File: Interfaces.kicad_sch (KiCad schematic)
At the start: 2 parts, among them J5 Conn_01x05_Pin, J6 Conn_01x05_Pin

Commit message: LCD connector, backlight, other work
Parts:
- removed J5: Conn_01x05_Pin, Connector_Molex:Molex_Micro-Fit_3.0_43650-0515_1x05_P3.00mm_Vertical, symbol Connector:Conn_01x05_Pin
- added J3: Conn_02x02_Counter_Clockwise, Connector_Molex:Molex_Micro-Fit_3.0_43045-0412_2x02_P3.00mm_Vertical, symbol Connector_Generic:Conn_02x02_Counter_Clockwise
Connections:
- net GND: now also J3.1 (Pin_1)
- new net +5V: J3.2 (Pin_2)
- new net IO_D0: J3.3 (Pin_3)
- new net IO_D1: J3.4 (Pin_4)
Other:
- moved on the sheet: J6

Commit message: preliminary complete schematic
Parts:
- removed J3: Conn_02x02_Counter_Clockwise, Connector_Molex:Molex_Micro-Fit_3.0_43045-0412_2x02_P3.00mm_Vertical, symbol Connector_Generic:Conn_02x02_Counter_Clockwise
- removed J6: Conn_01x05_Pin, Connector_Molex:Molex_Micro-Fit_3.0_43650-0515_1x05_P3.00mm_Vertical, symbol Connector:Conn_01x05_Pin
- added C12: 100n, Capacitor_SMD:C_0603_1608Metric_Pad1.08x0.95mm_HandSolder, symbol Device:C
- added C31, C32: 1u, Capacitor_SMD:C_0603_1608Metric_Pad1.08x0.95mm_HandSolder, symbol Device:C
- added J1: Conn_01x05_MountingPin, Connector_Molex:Molex_Micro-Fit_3.0_43650-0510_1x05-1MP_P3.00mm_Horizontal, symbol Connector_Generic_MountingPin:Conn_01x05_MountingPin
- added J3: Conn_01x04_MountingPin, Connector_Molex:Molex_Micro-Fit_3.0_43650-0410_1x04-1MP_P3.00mm_Horizontal, symbol Connector_Generic_MountingPin:Conn_01x04_MountingPin
- added J4: MSD-11-A, SamacSys_Parts:MSD11A, symbol SamacSys_Parts:MSD-11-A
- added J5: Conn_01x05_Pin, Connector_PinHeader_2.54mm:PinHeader_1x05_P2.54mm_Vertical, symbol Connector:Conn_01x05_Pin
- added R16, R17, R18, R19, R20, R22, R24, R27: 5.1k, Resistor_SMD:R_0603_1608Metric_Pad0.98x0.95mm_HandSolder, symbol Device:R
- added U6: TLV74033PDBVR, SamacSys_Parts:SOT95P280X145-5N, symbol SamacSys_Parts:TLV74033PDBVR
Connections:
- net +12V_IN: now also J1.2 (Pin_2)
- net +5V: now also C31.1, U6.1 (IN), U6.3 (EN)
- net +5V_BUS: now also J1.3 (Pin_3)
- net GND: now also C12.2, C31.2, C32.2, J1.1 (Pin_1), J1.MP (MountPin), J3.1 (Pin_1), J3.MP (MountPin), J4.G1 (GND_1), J4.G2 (GND_2), J4.P6 (VSS), J5.1 (Pin_1), U6.2 (GND)
- net PRIMARY_CAN+: now also J1.4 (Pin_4)
- net PRIMARY_CAN-: now also J1.5 (Pin_5)
- new net +3.3V: C12.1, J4.P4 (VDD), R16.2, R17.2, R18.2, R19.2, R20.2, R22.2, R24.2, R27.2
- new net +3.3V_AUX: C32.1, J3.2 (Pin_2), J5.2 (Pin_2), U6.5 (OUT)
- new net DPAD_A0: J3.3 (Pin_3)
- new net DPAD_A1: J3.4 (Pin_4)
- new net I2S_BCLK: J5.5 (Pin_5)
- new net I2S_SD: J5.4 (Pin_4)
- new net I2S_WS: J5.3 (Pin_3)
- new net SD_CD: J4.P9 (CD), R27.1
- new net SD_CLK: J4.P5 (CLK), R18.1
- new net SD_CMD: J4.P3 (CMD), R19.1
- new net SD_CS: J4.P2 (CD/DAT3), R20.1
- new net SD_D0: J4.P7 (DAT0), R17.1
- new net SD_D1: J4.P8 (DAT1), R16.1
- new net SD_D2: J4.P1 (DAT2), R22.1
- new net SD_WP: J4.P10 (WP), R24.1

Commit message: basic layout organization, fix +VDDA typo
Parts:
- renumbered C31 to C18, C32 to C19, C12 to C20, J5 to J4, J1 to J5, J4 to J6, R19 to R10, R20 to R11, R22 to R12, R24 to R13, R27 to R14, R16 to R7, R17 to R8, R18 to R9, U6 to U3
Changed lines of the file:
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@@
 		(on_board yes)
 		(dnp no)
-		(property "Reference" "J1"
+		(property "Reference" "J5"
 			(at 186.69 40.9955 0)
 			(effects
@@
 			(project ""
 				(path "/f2bb7816-6b2a-47fd-8906-eb4aedd6f9e6/61479cd4-0d84-48d3-a2a5-35c815fbc6c8"
-					(reference "J1")
+					(reference "J5")
 					(unit 1)
 				)
@@
 		(dnp no)
 		(fields_autoplaced yes)
-		(property "Reference" "#PWR026"
+		(property "Reference" "#PWR027"
 			(at 222.25 48.26 0)
 			(effects
@@
 			(project "LV3-Core"
 				(path "/f2bb7816-6b2a-47fd-8906-eb4aedd6f9e6/61479cd4-0d84-48d3-a2a5-35c815fbc6c8"
-					(reference "#PWR026")
+					(reference "#PWR027")
 					(unit 1)
 				)
@@
 		(dnp no)
 		(fields_autoplaced yes)
-		(property "Reference" "#PWR055"
+		(property "Reference" "#PWR032"
 			(at 222.25 78.74 0)
 			(effects
@@
 			(project "LV3-Dash"
 				(path "/f2bb7816-6b2a-47fd-8906-eb4aedd6f9e6/61479cd4-0d84-48d3-a2a5-35c815fbc6c8"
-					(reference "#PWR055")
+					(reference "#PWR032")
 					(unit 1)
 				)
@@
 		(dnp no)
 		(fields_autoplaced yes)
-		(property "Reference" "R18"
+		(property "Reference" "R9"
 			(at 118.11 104.1399 0)
 			(effects
@@
 			(project "LV3-Dash"
 				(path "/f2bb7816-6b2a-47fd-8906-eb4aedd6f9e6/61479cd4-0d84-48d3-a2a5-35c815fbc6c8"
-					(reference "R18")
+					(reference "R9")
 					(unit 1)
 				)
@@
 		(dnp no)
 		(fields_autoplaced yes)
-		(property "Reference" "#PWR060"
+		(property "Reference" "#PWR028"
 			(at 120.65 54.61 0)
 			(effects
@@
 			(project "LV3-Dash"
 				(path "/f2bb7816-6b2a-47fd-8906-eb4aedd6f9e6/61479cd4-0d84-48d3-a2a5-35c815fbc6c8"
-					(reference "#PWR060")
+					(reference "#PWR028")
 					(unit 1)
 				)
@@
 		(dnp no)
 		(fields_autoplaced yes)
-		(property "Reference" "R27"
+		(property "Reference" "R14"
 			(at 165.1 104.1399 0)
 			(effects
@@
 			(project "LV3-Dash"
 				(path "/f2bb7816-6b2a-47fd-8906-eb4aedd6f9e6/61479cd4-0d84-48d3-a2a5-35c815fbc6c8"
-					(reference "R27")
+					(reference "R14")
 					(unit 1)
 				)
@@
 		(dnp no)
 		(fields_autoplaced yes)
-		(property "Reference" "R19"
+		(property "Reference" "R10"
 			(at 128.27 104.1399 0)
 			(effects
@@
 			(project "LV3-Dash"
 				(path "/f2bb7816-6b2a-47fd-8906-eb4aedd6f9e6/61479cd4-0d84-48d3-a2a5-35c815fbc6c8"
-					(reference "R19")
+					(reference "R10")
 					(unit 1)
 				)
@@
 		(dnp no)
 		(fields_autoplaced yes)
-		(property "Reference" "J5"
+		(property "Reference" "J4"
 			(at 239.395 30.48 0)
 			(effects
@@
 			(project ""
 				(path "/f2bb7816-6b2a-47fd-8906-eb4aedd6f9e6/61479cd4-0d84-48d3-a2a5-35c815fbc6c8"
-					(reference "J5")
+					(reference "J4")
 					(unit 1)
 				)
@@
 		(dnp no)
 		(fields_autoplaced yes)
-		(property "Reference" "U6"
+		(property "Reference" "U3"
 			(at 203.2 64.77 0)
 			(effects
@@
 			(project "LV3-Dash"
 				(path "/f2bb7816-6b2a-47fd-8906-eb4aedd6f9e6/61479cd4-0d84-48d3-a2a5-35c815fbc6c8"
-					(reference "U6")
+					(reference "U3")
 					(unit 1)
 				)
@@
 		(dnp no)
 		(fields_autoplaced yes)
-		(property "Reference" "#PWR050"
+		(property "Reference" "#PWR029"
 			(at 259.08 54.61 0)
 			(effects
@@
 			(project "LV3-Dash"
 				(path "/f2bb7816-6b2a-47fd-8906-eb4aedd6f9e6/61479cd4-0d84-48d3-a2a5-35c815fbc6c8"
-					(reference "#PWR050")
+					(reference "#PWR029")
 					(unit 1)
 				)
@@
 		(dnp no)
 		(fields_autoplaced yes)
-		(property "Reference" "J4"
+		(property "Reference" "J6"
 			(at 57.15 104.14 0)
 			(effects
@@
 			(project "LV3-Dash"
 				(path "/f2bb7816-6b2a-47fd-8906-eb4aedd6f9e6/61479cd4-0d84-48d3-a2a5-35c815fbc6c8"
-					(reference "J4")
+					(reference "J6")
 					(unit 1)
 				)
@@
 		(dnp no)
 		(fields_autoplaced yes)
-		(property "Reference" "#PWR015"
+		(property "Reference" "#PWR023"
 			(at 135.89 35.56 0)
 			(effects
@@
 			(project "LV3-Dash"
 				(path "/f2bb7816-6b2a-47fd-8906-eb4aedd6f9e6/61479cd4-0d84-48d3-a2a5-35c815fbc6c8"
-					(reference "#PWR015")
+					(reference "#PWR023")
 					(unit 1)
 				)
@@
 		(dnp no)
 		(fields_autoplaced yes)
-		(property "Reference" "#PWR054"
+		(property "Reference" "#PWR033"
 			(at 187.96 88.9 0)
 			(effects
@@
 			(project "LV3-Dash"
 				(path "/f2bb7816-6b2a-47fd-8906-eb4aedd6f9e6/61479cd4-0d84-48d3-a2a5-35c815fbc6c8"
-					(reference "#PWR054")
+					(reference "#PWR033")
 					(unit 1)
 				)
@@
 		(dnp no)
 		(fields_autoplaced yes)
-		(property "Reference" "R24"
+		(property "Reference" "R13"
 			(at 156.21 104.1399 0)
 			(effects
@@
 			(project "LV3-Dash"
 				(path "/f2bb7816-6b2a-47fd-8906-eb4aedd6f9e6/61479cd4-0d84-48d3-a2a5-35c815fbc6c8"
-					(reference "R24")
+					(reference "R13")
 					(unit 1)
 				)
@@
 		(dnp no)
 		(fields_autoplaced yes)
-		(property "Reference" "C32"
+		(property "Reference" "C19"
 			(at 226.06 77.4699 0)
 			(effects
@@
 			(project "LV3-Dash"
 				(path "/f2bb7816-6b2a-47fd-8906-eb4aedd6f9e6/61479cd4-0d84-48d3-a2a5-35c815fbc6c8"
-					(reference "C32")
+					(reference "C19")
 					(unit 1)
 				)
@@
 		(dnp no)
 		(fields_autoplaced yes)
-		(property "Reference" "R17"
+		(property "Reference" "R8"
 			(at 109.22 104.1399 0)
 			(effects
@@
 			(project "LV3-Dash"
 				(path "/f2bb7816-6b2a-47fd-8906-eb4aedd6f9e6/61479cd4-0d84-48d3-a2a5-35c815fbc6c8"
-					(reference "R17")
+					(reference "R8")
 					(unit 1)
 				)
@@
 		(dnp no)
 		(fields_autoplaced yes)
-		(property "Reference" "R20"
+		(property "Reference" "R11"
 			(at 138.43 104.1399 0)
 			(effects
@@
 			(project "LV3-Dash"
 				(path "/f2bb7816-6b2a-47fd-8906-eb4aedd6f9e6/61479cd4-0d84-48d3-a2a5-35c815fbc6c8"
-					(reference "R20")
+					(reference "R11")
 					(unit 1)
 				)
@@
 		(dnp no)
 		(fields_autoplaced yes)
-		(property "Reference" "#PWR051"
+		(property "Reference" "#PWR031"
 			(at 170.18 76.2 0)
 			(effects
@@
 			(project "LV3-Dash"
 				(path "/f2bb7816-6b2a-47fd-8906-eb4aedd6f9e6/61479cd4-0d84-48d3-a2a5-35c815fbc6c8"
-					(reference "#PWR051")
+					(reference "#PWR031")
 					(unit 1)
 				)
@@
 		(dnp no)
 		(fields_autoplaced yes)
-		(property "Reference" "#PWR061"
+		(property "Reference" "#PWR030"
 			(at 189.23 58.42 0)
 			(effects
@@
 			(project "LV3-Dash"
 				(path "/f2bb7816-6b2a-47fd-8906-eb4aedd6f9e6/61479cd4-0d84-48d3-a2a5-35c815fbc6c8"
-					(reference "#PWR061")
+					(reference "#PWR030")
 					(unit 1)
 				)
@@
 		(dnp no)
 		(fields_autoplaced yes)
-		(property "Reference" "#PWR027"
+		(property "Reference" "#PWR036"
 			(at 34.29 124.46 0)
 			(effects
@@
 			(project "LV3-Dash"
 				(path "/f2bb7816-6b2a-47fd-8906-eb4aedd6f9e6/61479cd4-0d84-48d3-a2a5-35c815fbc6c8"
-					(reference "#PWR027")
+					(reference "#PWR036")
 					(unit 1)
 				)
@@
 		(dnp no)
 		(fields_autoplaced yes)
-		(property "Reference" "#PWR046"
+		(property "Reference" "#PWR022"
 			(at 261.62 34.29 0)
 			(effects
@@
 			(project "LV3-Dash"
 				(path "/f2bb7816-6b2a-47fd-8906-eb4aedd6f9e6/61479cd4-0d84-48d3-a2a5-35c815fbc6c8"
-					(reference "#PWR046")
+					(reference "#PWR022")
 					(unit 1)
 				)
@@
 		(dnp no)
 		(fields_autoplaced yes)
-		(property "Reference" "C12"
+		(property "Reference" "C20"
 			(at 77.47 96.5199 0)
 			(effects
@@
 			(project "LV3-Dash"
 				(path "/f2bb7816-6b2a-47fd-8906-eb4aedd6f9e6/61479cd4-0d84-48d3-a2a5-35c815fbc6c8"
-					(reference "C12")
+					(reference "C20")
 					(unit 1)
 				)
@@
 		(dnp no)
 		(fields_autoplaced yes)
-		(property "Reference" "#PWR029"
+		(property "Reference" "#PWR035"
 			(at 81.28 107.95 0)
 			(effects
@@
 			(project "LV3-Dash"
 				(path "/f2bb7816-6b2a-47fd-8906-eb4aedd6f9e6/61479cd4-0d84-48d3-a2a5-35c815fbc6c8"
-					(reference "#PWR029")
+					(reference "#PWR035")
 					(unit 1)
 				)
@@
 		(dnp no)
 		(fields_autoplaced yes)
-		(property "Reference" "#PWR028"
+		(property "Reference" "#PWR034"
 			(at 87.63 97.79 0)
 			(effects
@@
 			(project "LV3-Dash"
 				(path "/f2bb7816-6b2a-47fd-8906-eb4aedd6f9e6/61479cd4-0d84-48d3-a2a5-35c815fbc6c8"
-					(reference "#PWR028")
+					(reference "#PWR034")
 					(unit 1)
 				)
@@
 		(dnp no)
 		(fields_autoplaced yes)
-		(property "Reference" "#PWR045"
+		(property "Reference" "#PWR037"
 			(at 91.44 144.78 0)
 			(effects
@@
 			(project "LV3-Dash"
 				(path "/f2bb7816-6b2a-47fd-8906-eb4aedd6f9e6/61479cd4-0d84-48d3-a2a5-35c815fbc6c8"
-					(reference "#PWR045")
+					(reference "#PWR037")
 					(unit 1)
 				)
@@
 		(dnp no)
 		(fields_autoplaced yes)
-		(property "Reference" "#PWR013"
+		(property "Reference" "#PWR026"
 			(at 153.67 44.45 0)
 			(effects
@@
 			(project "LV3-Dash"
 				(path "/f2bb7816-6b2a-47fd-8906-eb4aedd6f9e6/61479cd4-0d84-48d3-a2a5-35c815fbc6c8"
-					(reference "#PWR013")
+					(reference "#PWR026")
 					(unit 1)
 				)
@@
 		(dnp no)
 		(fields_autoplaced yes)
-		(property "Reference" "R22"
+		(property "Reference" "R12"
 			(at 147.32 104.1399 0)
 			(effects
@@
 			(project "LV3-Dash"
 				(path "/f2bb7816-6b2a-47fd-8906-eb4aedd6f9e6/61479cd4-0d84-48d3-a2a5-35c815fbc6c8"
-					(reference "R22")
+					(reference "R12")
 					(unit 1)
 				)
@@
 		(dnp no)
 		(fields_autoplaced yes)
-		(property "Reference" "R16"
+		(property "Reference" "R7"
 			(at 99.06 104.1399 0)
 			(effects
@@
 			(project "LV3-Dash"
 				(path "/f2bb7816-6b2a-47fd-8906-eb4aedd6f9e6/61479cd4-0d84-48d3-a2a5-35c815fbc6c8"
-					(reference "R16")
+					(reference "R7")
 					(unit 1)
 				)
@@
 		(dnp no)
 		(fields_autoplaced yes)
-		(property "Reference" "C31"
+		(property "Reference" "C18"
 			(at 179.07 74.9299 0)
 			(effects
@@
 			(project "LV3-Dash"
 				(path "/f2bb7816-6b2a-47fd-8906-eb4aedd6f9e6/61479cd4-0d84-48d3-a2a5-35c815fbc6c8"
-					(reference "C31")
-					(unit 1)
-				)
+					(reference "C18")
+					(unit 1)
+				)

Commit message: finalize connector placement, modify layout
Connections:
- net +3.3V_AUX: no longer J4.2 (Pin_2)
- net +5V: now also J4.2 (Pin_2)
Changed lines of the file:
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@@
 			)
 		)
-		(property "Value" "+3.3V_AUX"
-			(at 261.62 25.4 0)
+		(property "Value" "+5V"
+			(at 264.16 29.2099 0)
 			(effects
 				(font
 					(size 1.27 1.27)
 				)
+				(justify left)
 			)
 		)

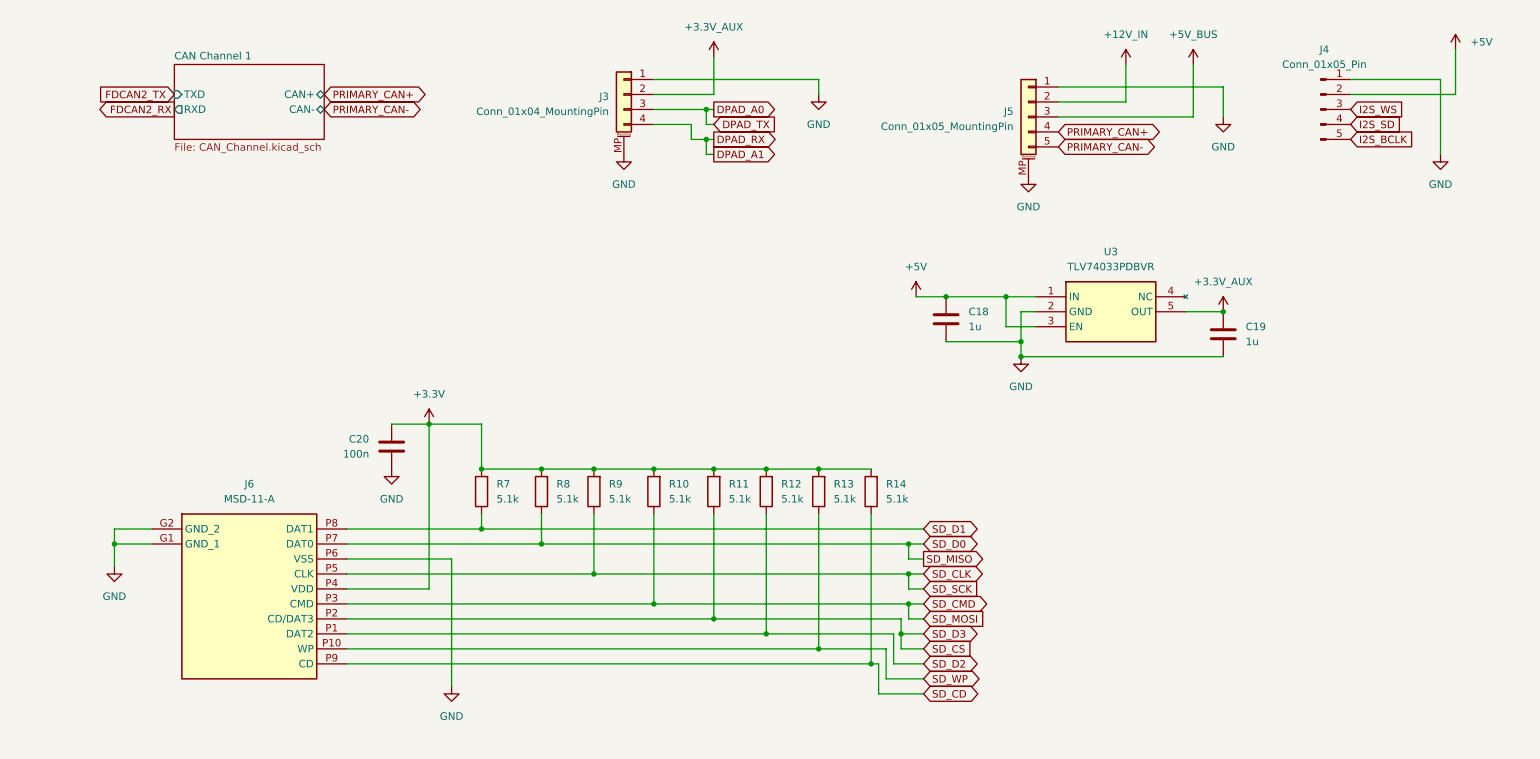
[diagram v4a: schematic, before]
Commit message: 3.3v regulator changes, GPIO output fixes, layout changes
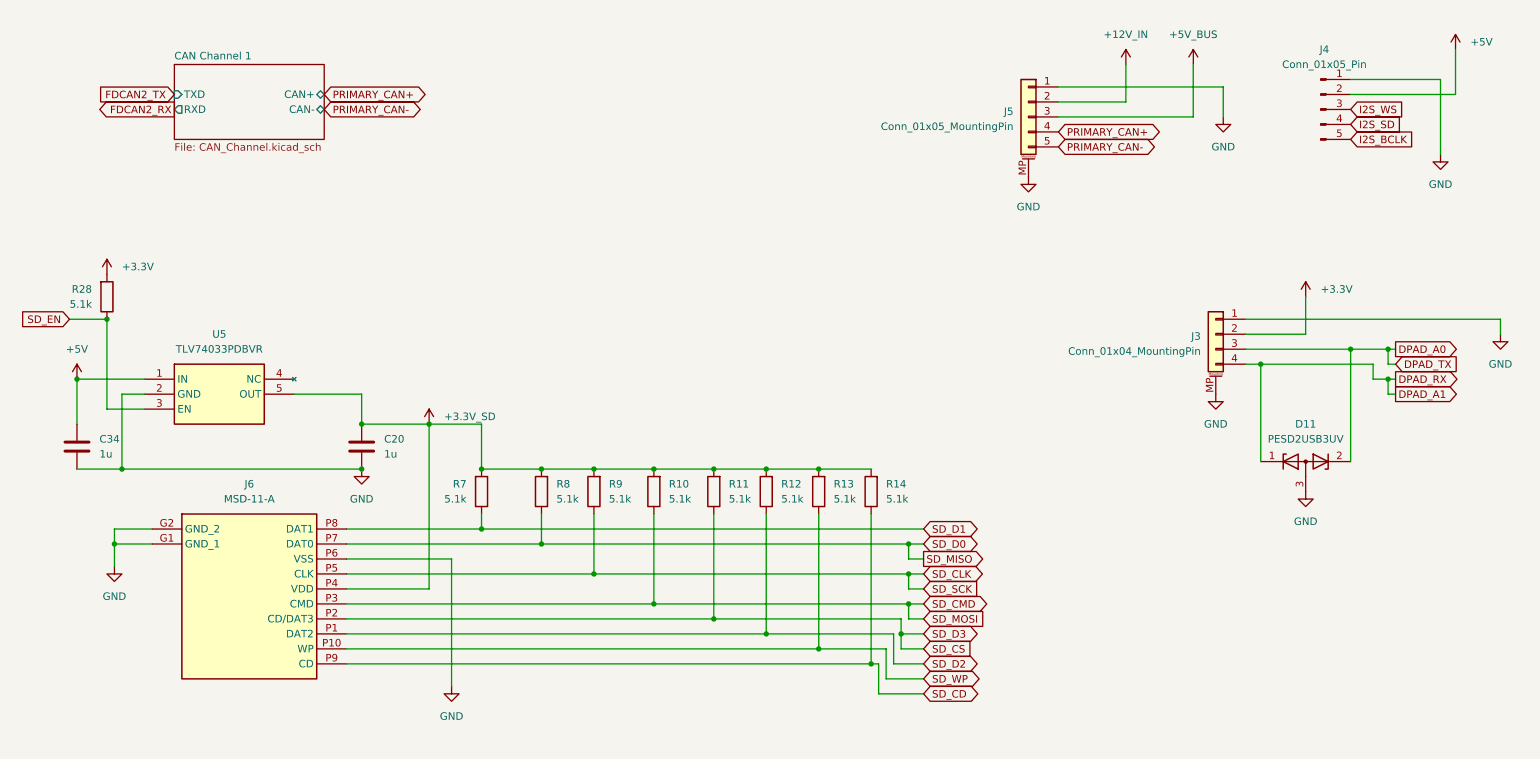
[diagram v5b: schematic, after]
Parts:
- removed C18, C19: 1u, Capacitor_SMD:C_0603_1608Metric_Pad1.08x0.95mm_HandSolder, symbol Device:C
- removed U3: TLV74033PDBVR, SamacSys_Parts:SOT95P280X145-5N, symbol SamacSys_Parts:TLV74033PDBVR
- added C34: 1u, Capacitor_SMD:C_0603_1608Metric_Pad1.08x0.95mm_HandSolder, symbol Device:C
- added D11: PESD2USB3UV, Package_TO_SOT_SMD:SOT-23W, symbol Device:D_Zener_Dual_CommonAnode_KKA
- added R28: 5.1k, Resistor_SMD:R_0603_1608Metric_Pad0.98x0.95mm_HandSolder, symbol Device:R
- added U5: TLV74033PDBVR, SamacSys_Parts:SOT95P280X145-5N, symbol SamacSys_Parts:TLV74033PDBVR
- C20: value 100n -> 1u
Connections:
- net +3.3V_AUX is gone; now on net +3.3V: J3.2 (Pin_2)
- net +3.3V: now also R28.2; no longer C20.1, J6.P4 (VDD), R10.2, R11.2, R12.2, R13.2, R14.2, R7.2, R8.2, R9.2
- net +5V: now also C34.1, U5.1 (IN)
- net DPAD_A0: now also D11.2 (K)
- net DPAD_A1: now also D11.1 (K)
- net GND: now also C34.2, D11.3 (A), U5.2 (GND)
- new net +3.3V_SD: C20.1, J6.P4 (VDD), R10.2, R11.2, R12.2, R13.2, R14.2, R7.2, R8.2, R9.2, U5.5 (OUT)
- new net SD_EN: R28.1, U5.3 (EN)
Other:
- moved on the sheet: C20, J3, R7

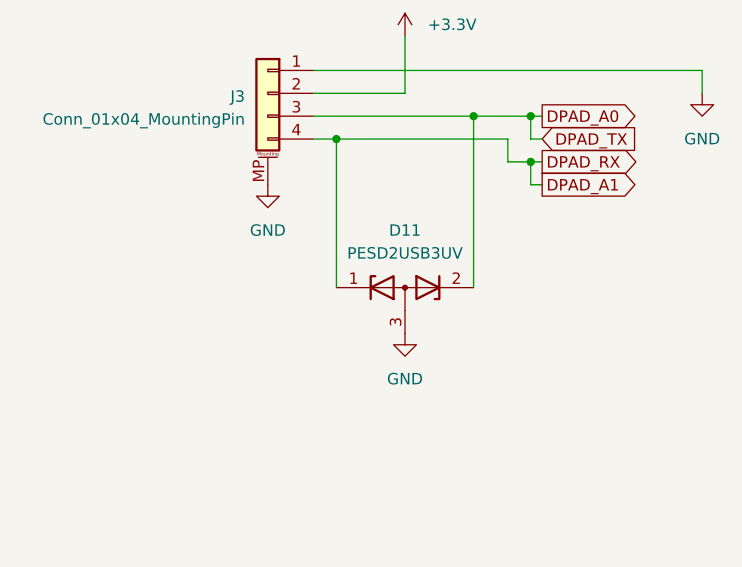
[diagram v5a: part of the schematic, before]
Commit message: some preliminary routing
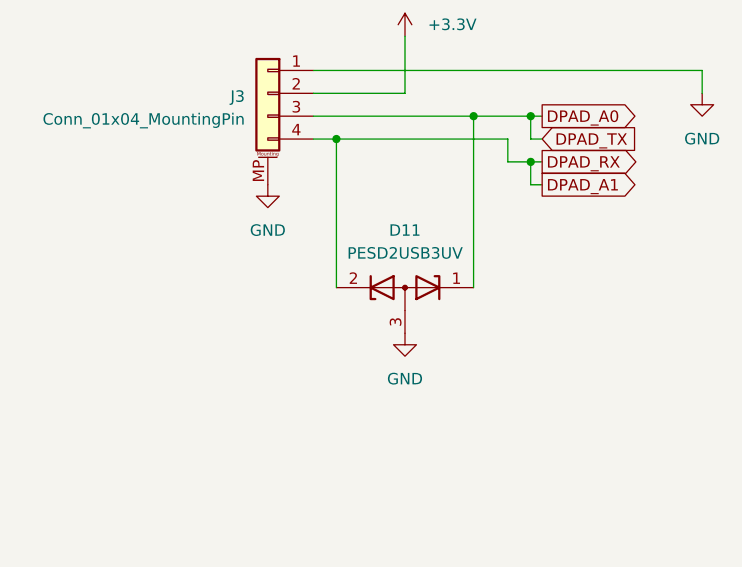
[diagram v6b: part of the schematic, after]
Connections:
- net DPAD_A0: now also D11.1 (K); no longer D11.2 (K)
- net DPAD_A1: now also D11.2 (K); no longer D11.1 (K)
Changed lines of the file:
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@@
 		(lib_id "Device:D_Zener_Dual_CommonAnode_KKA")
 		(at 236.22 100.33 0)
+		(mirror y)
 		(unit 1)
 		(exclude_from_sim no)
@@
 		(on_board yes)
 		(dnp no)
-		(fields_autoplaced yes)
 		(property "Reference" "D11"
 			(at 236.22 93.98 0)

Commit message: r1 final (see changelog.md)
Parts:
- removed J4: Conn_01x05_Pin, Connector_PinHeader_2.54mm:PinHeader_1x05_P2.54mm_Vertical, symbol Connector:Conn_01x05_Pin
- added J4: Conn_01x08_Pin, Connector_PinHeader_2.54mm:PinHeader_1x08_P2.54mm_Vertical, symbol Connector:Conn_01x08_Pin
- added J8: Conn_01x03_Pin, Connector_PinHeader_2.54mm:PinHeader_1x03_P2.54mm_Vertical, symbol Connector:Conn_01x03_Pin
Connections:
- net +5V: now also J4.2 (Pin_2)
- net GND: now also J4.1 (Pin_1), J8.1 (Pin_1)
- net I2S_BCLK: now also J4.5 (Pin_5)
- net I2S_SD: now also J4.4 (Pin_4)
- net I2S_WS: now also J4.3 (Pin_3)
- new net CTP_SCL: J8.3 (Pin_3)
- new net CTP_SDA: J8.2 (Pin_2)
- new net SAI_FS: J4.6 (Pin_6)
- new net SAI_SCK: J4.7 (Pin_7)
- new net SAI_SD: J4.8 (Pin_8)
